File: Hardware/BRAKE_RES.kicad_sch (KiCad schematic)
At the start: 12 parts, among them Q13 CSD19532Q5B, Q15 CSD19532Q5B, U58 EG2104

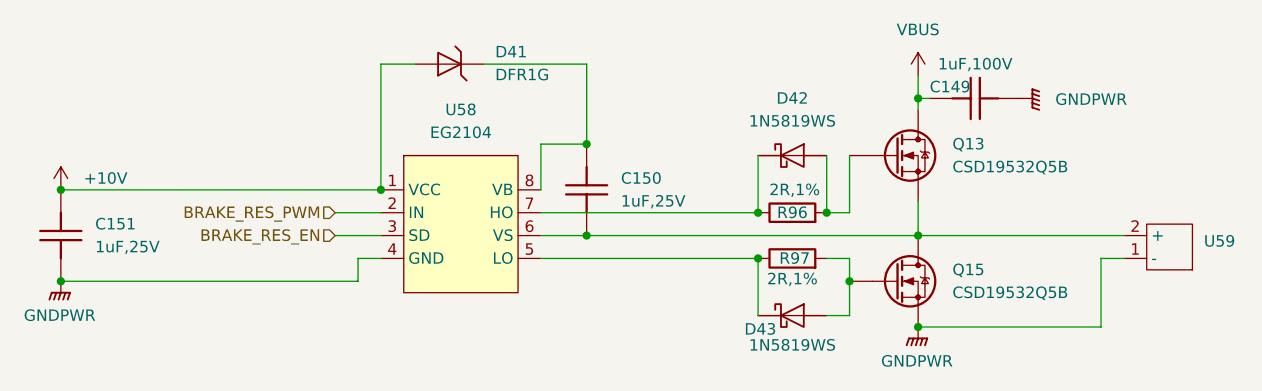
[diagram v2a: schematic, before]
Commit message: PCB修改栅极电阻，增加上侧RC吸收电路，同步修改软件死区时间到150ns
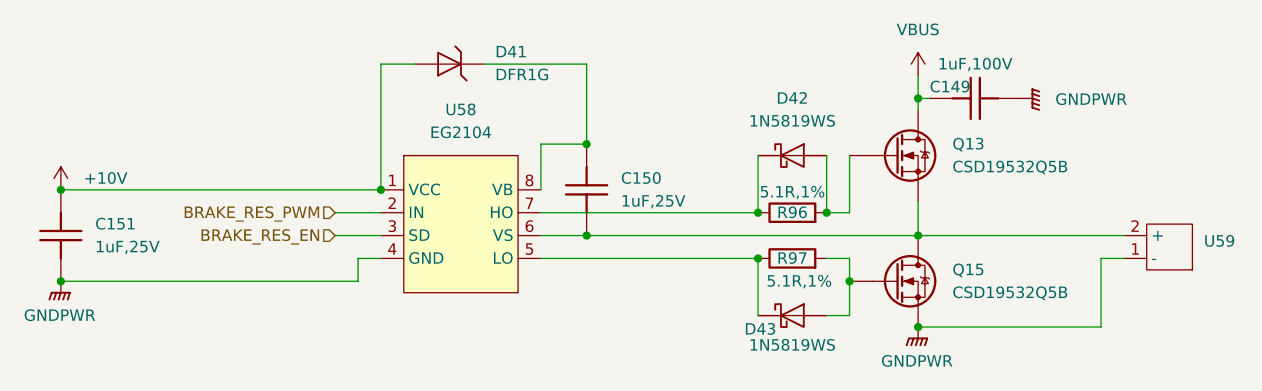
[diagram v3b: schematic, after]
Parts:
- R96, R97: value 2R,1% -> 5.1R,1%; symbol HPM6280Foc:0402WGF200KTCE -> HPM6280Foc:0402WGF510KTCE; 立创编号 C270630 -> C25128
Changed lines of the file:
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@@
 	)
 	(symbol
-		(lib_id "HPM6280Foc:0402WGF200KTCE")
+		(lib_id "HPM6280Foc:0402WGF510KTCE")
 		(at 165.1 92.71 0)
 		(unit 1)
@@
 			)
 		)
-		(property "Value" "2R,1%"
-			(at 165.354 90.17 0)
+		(property "Value" "5.1R,1%"
+			(at 165.1 90.424 0)
 			(effects
 				(font
@@
 			)
 		)
-		(property "Description" "2Ω ±1% 62.5mW 厚膜电阻"
+		(property "Description" "5.1Ω ±1% 62.5mW 厚膜电阻"
 			(at 165.1 92.71 0)
 			(effects
@@
 			)
 		)
-		(property "立创编号" "C270630"
+		(property "立创编号" "C25128"
 			(at 165.1 92.71 0)
 			(effects
@@
 	)
 	(symbol
-		(lib_id "HPM6280Foc:0402WGF200KTCE")
+		(lib_id "HPM6280Foc:0402WGF510KTCE")
 		(at 165.1 97.79 0)
 		(unit 1)
@@
 		(dnp no)
 		(property "Reference" "R97"
-			(at 165.354 97.79 0)
-			(effects
-				(font
-					(size 1.27 1.27)
-				)
-			)
-		)
-		(property "Value" "2R,1%"
-			(at 165.1 100.076 0)
+			(at 165.1 97.79 0)
+			(effects
+				(font
+					(size 1.27 1.27)
+				)
+			)
+		)
+		(property "Value" "5.1R,1%"
+			(at 165.862 100.33 0)
 			(effects
 				(font
@@
 			)
 		)
-		(property "Description" "2Ω ±1% 62.5mW 厚膜电阻"
+		(property "Description" "5.1Ω ±1% 62.5mW 厚膜电阻"
 			(at 165.1 97.79 0)
 			(effects
@@
 			)
 		)
-		(property "立创编号" "C270630"
+		(property "立创编号" "C25128"
 			(at 165.1 97.79 0)
 			(effects
